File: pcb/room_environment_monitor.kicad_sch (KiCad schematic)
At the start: 33 parts, among them J1 Conn_01x02_Pin, J3 Conn_01x06_Socket, P1 USB_C_Plug_USB2.0, Q2 BSS138, SW1 SW_SPST, U1 ATECC608A-MAHDA, U2 ESP32-C3-MINI-1, U5 AP2112K-3.3

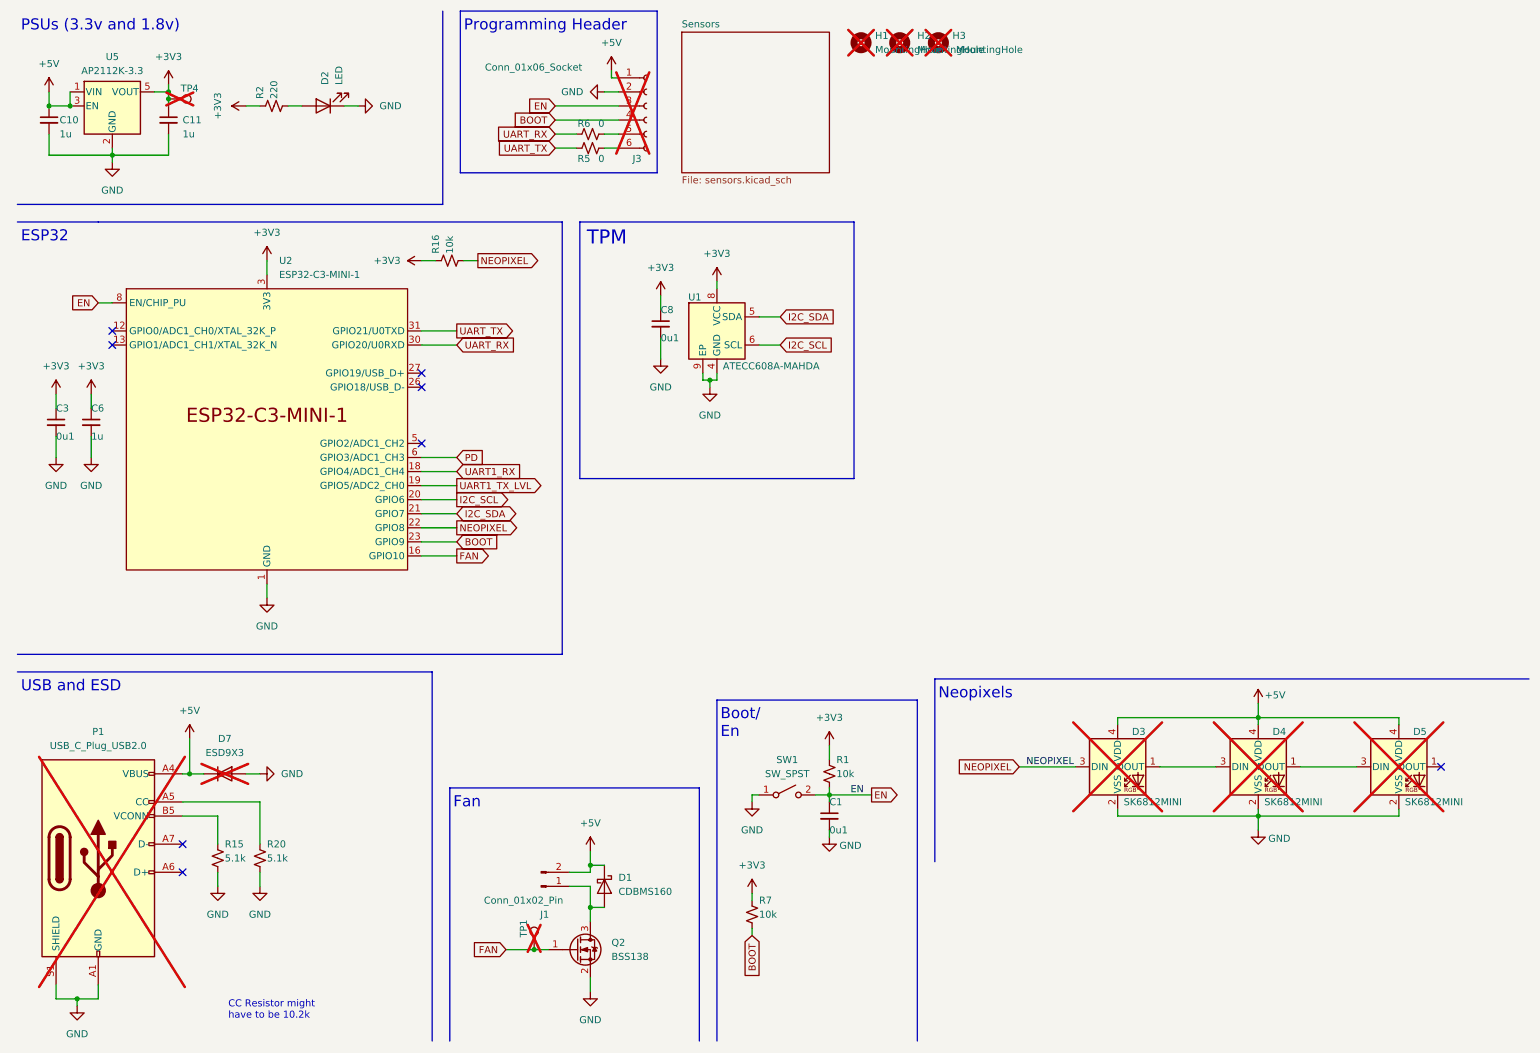
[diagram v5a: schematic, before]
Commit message: do the reroute for the larger ESP32 module
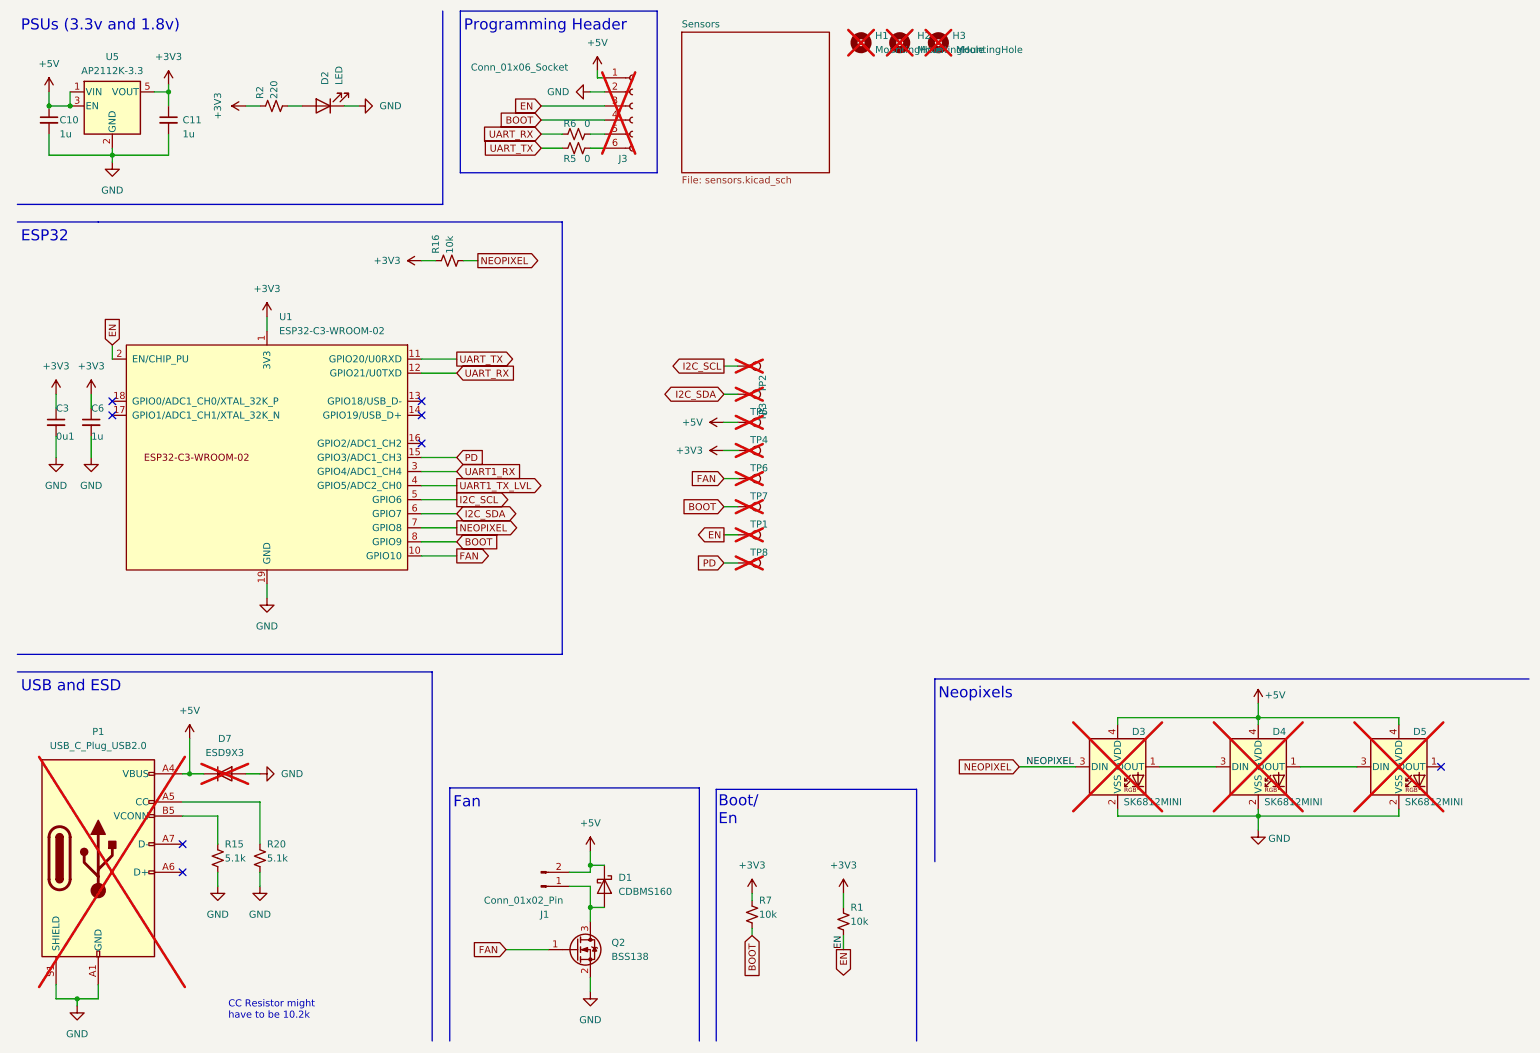
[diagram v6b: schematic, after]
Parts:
- removed C1, C8: 0u1, Capacitor_SMD:C_0603_1608Metric, symbol Device:C_Small
- removed SW1: SW_SPST, Button_Switch_SMD:SW_Push_1P1T_NO_CK_KMR2, symbol Switch:SW_SPST
- removed U1: ATECC608A-MAHDA, Package_DFN_QFN:DFN-8-1EP_3x2mm_P0.5mm_EP1.3x1.5mm, symbol Security:ATECC608A-MAHDA
- removed U2: ESP32-C3-MINI-1, PCM_Espressif:ESP32-C3-MINI-1, symbol PCM_Espressif:ESP32-C3-MINI-1
- added TP2, TP3, TP5, TP6, TP7, TP8: TestPoint, TestPoint:TestPoint_Pad_D1.0mm, symbol Connector:TestPoint
- added U1: ESP32-C3-WROOM-02, PCM_Espressif:ESP32-C3-WROOM-02, symbol PCM_Espressif:ESP32-C3-WROOM-02
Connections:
- net +3V3: now also U1.1 (3V3)
- net +5V: now also TP5.1
- net BOOT: now also TP7.1, U1.8 (GPIO9)
- net EN: now also TP1.1, U1.2 (EN/CHIP_PU)
- net FAN: now also TP6.1, U1.10 (GPIO10); no longer TP1.1
- net GND: now also U1.19 (GND), U1.9 (GND)
- net I2C_SCL: now also TP2.1, U1.5 (GPIO6)
- net I2C_SDA: now also TP3.1, U1.6 (GPIO7)
- net NEOPIXEL: now also U1.7 (GPIO8)
- net PD: now also TP8.1, U1.15 (GPIO3/ADC1_CH3)
- net UART1_RX: now also U1.3 (GPIO4/ADC1_CH4)
- net UART1_TX_LVL: now also U1.4 (GPIO5/ADC2_CH0)
- net UART_RX: now also U1.12 (GPIO21/U0TXD)
- net UART_TX: now also U1.11 (GPIO20/U0RXD)
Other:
- note removed: "TPM"
- moved on the sheet: J3, R1, R5, R6

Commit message: cleanup files
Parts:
- removed R16: 10k, Resistor_SMD:R_0603_1608Metric, symbol Device:R_Small_US
- added Q3: BSS138, Package_TO_SOT_SMD:SOT-23, symbol Transistor_FET:BSS138
- added R17, R18: 10k, Resistor_SMD:R_0603_1608Metric, symbol Device:R_Small_US
- D3, D4, D5: footprint LED_SMD:LED_SK6812MINI_PLCC4_3.5x3.5mm_P1.75mm -> LED_SMD:LED_WS2812B-2020_PLCC4_2.0x2.0mm
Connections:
- net +3V3: now also Q3.1 (G), R18.1
- net +5V: now also R17.1
- net NEOPIXEL: now also Q3.2 (S), R18.2; no longer D3.3 (DIN)
- new net NEOPIXEL_LVL: D3.3 (DIN), Q3.3 (D), R17.2
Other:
- note added: "Level shifter for the 3.3 logic to the LL of the LEDS: VDD - 0.3V (4.7)"
- note added: "Test Points"
- moved on the sheet: D3, D4, D5, TP1, TP2, TP3, TP4, TP5, TP6, TP7, TP8
